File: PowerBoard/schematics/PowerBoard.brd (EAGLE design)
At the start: 200 x 100 mm, 28 parts, among them IC1 LM317MB, IC2 LM317MB, T1 TIP31C, T2 TIP31C, T3 TIP32C, X1 22-27-2031-03, X2 22-27-2031-03

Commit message: power distribution with regulators and capacitance multipliers
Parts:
- removed C1, C2: .1uF, resistor:C025-025X050
- removed C3: 1uF, resistor:E3,5-8
- removed C4, C5, C6: 100uF, resistor:E3,5-8
- removed IC3: (no value), v-reg:337TL
- removed R4: 2K, resistor:0207/7
- removed R5: 730R, resistor:0207/7
- removed R6: 1.35K, resistor:0207/7
- removed R7, R8, R9: 1K, resistor:0207/7
- added C100, C200: .1uF, rcl:C0603
- added C101, C201, C301: 100uF, rcl:153CLV-0810
- added C300: 1uF, rcl:153CLV-0810
- added IC4: 337IMP, linear:SOT223
- added LED1, LED2, LED3: (no value), led:CHIPLED_1206
- added R100: 2K, Rebel:0603
- added R101, R201: 220R, Rebel:0603
- added R102, R202, R302: 1K, Rebel:0603
- added R200: 730R, Rebel:0603
- added R300: 1.35K, Rebel:0603
- added R301: 150R, Rebel:0603
- IC1, IC2: value LM317MB -> LM317MSTT3; device v-reg:TO220L1 -> v-reg:SOT223
- R1, R2: value 220R -> 1K; device resistor:0207/7 -> Rebel:0603
- R3: value 150R -> 1K; device resistor:0207/7 -> Rebel:0603
- moved R3 203.6 mm to (147.3, 2.54), turned to 180 degrees
- moved R2 192.8 mm to (147.3, 6.35), turned to 180 degrees
- moved R1 182.0 mm to (147.3, 10.2), turned to 180 degrees
- moved T1 43.4 mm to (17.8, 20.3)
- moved IC2 42.6 mm to (59.7, 31.8)
- moved T3 38.2 mm to (95.2, 20.3)
- moved IC1 6.35 mm to (12.7, 31.8)
- moved T2 4.02 mm to (55.9, 20.3)
- moved X1 1.27 mm to (3.81, 6.35)
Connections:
- new net N$1: LED1.A, R1.2
- new net N$2: LED2.A, R2.2
- new net N$9: LED3.C, R3.2
- net +12V: now also LED1.C
- net +15V: now also C100.1, C200.1; no longer C1.1, C2.1
- net +5V: now also LED2.C
- net -12V: now also LED3.A
- net -15V: now also C300.-, IC4.4; no longer C3.-, IC3.2
- net 0V: now also C100.2, C101.-, C200.2, C201.-, C300.+, C301.-, R1.1, R100.1, R2.1, R200.1, R3.1, R300.2; no longer C1.2, C2.2, C3.+, C4.-, C5.-, C6.-, R4.1, R5.1, R6.2
- net N$10: now also C101.+, R102.1; no longer C4.+, R7.1
- net N$11: now also C201.+, R202.1; no longer C5.+, R8.1
- net N$12: now also C301.+, R302.2; no longer C6.+, R9.2
- net N$3: now also R100.2, R101.1; no longer R1.1, R4.2
- net N$4: now also R200.2, R201.1; no longer R2.1, R5.2
- net N$5: now also IC4.1, R300.1, R301.2; no longer IC3.1, R3.2, R6.1
- net N$6: now also IC1.4, R101.2, R102.2; no longer IC1.2, R1.2, R7.2
- net N$7: now also IC2.4, R201.2, R202.2; no longer IC2.2, R2.2, R8.2
- net N$8: now also IC4.3, R301.1, R302.1; no longer IC3.3, R3.1, R9.1
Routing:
- added copper zone on layer 1, net N$13
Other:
- board size 200 x 100 mm -> 200 x 53 mm

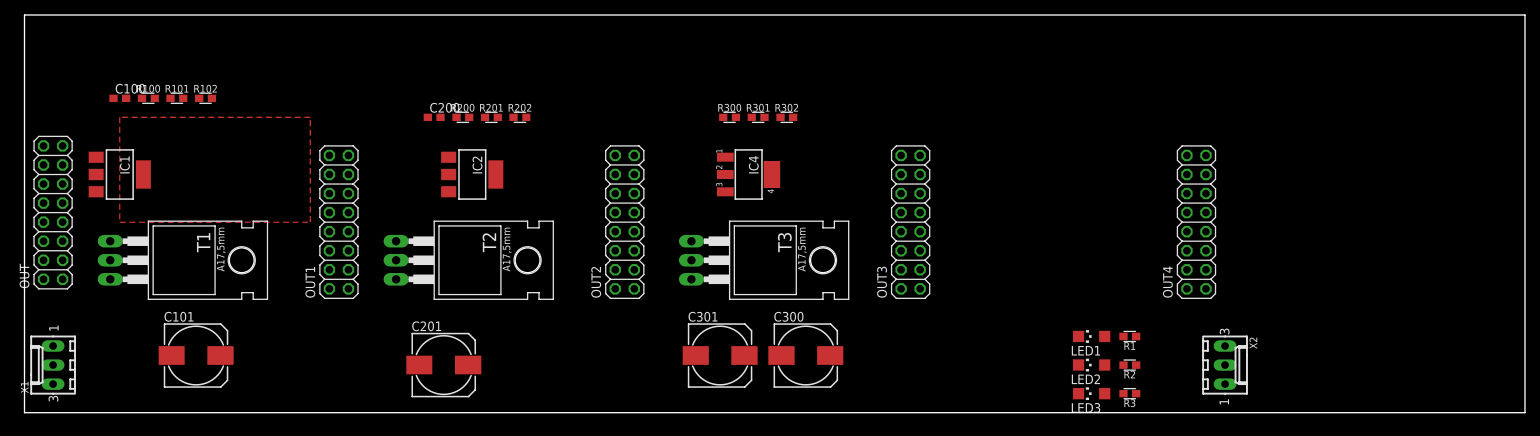
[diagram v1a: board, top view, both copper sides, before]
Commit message: changed to DPACK, 140mm long board
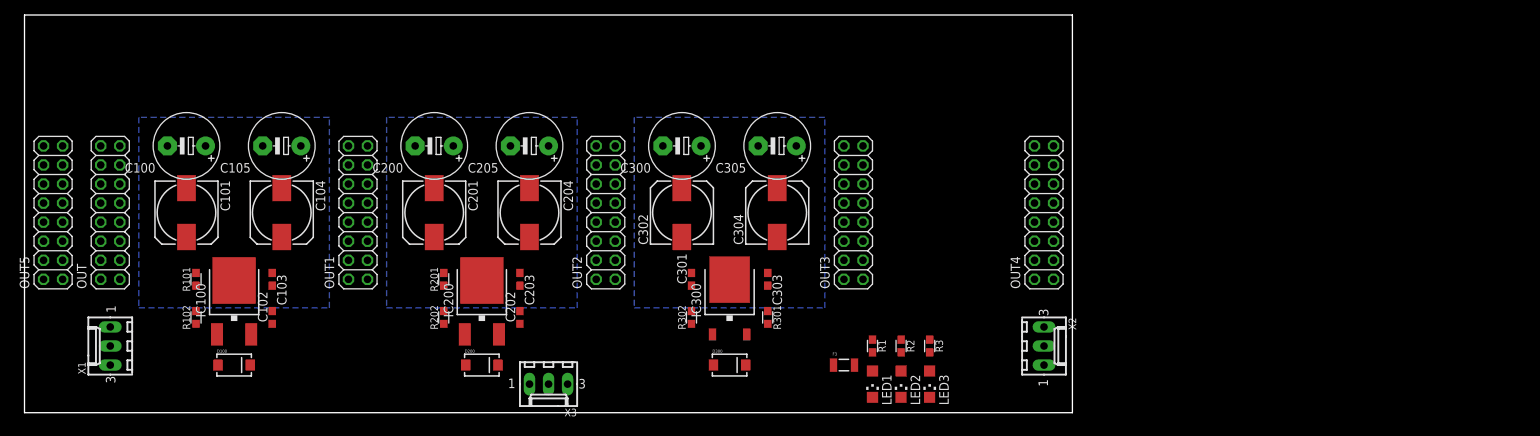
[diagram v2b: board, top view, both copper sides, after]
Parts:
- removed IC1, IC2: LM317MSTT3, v-reg:SOT223
- removed IC4: 337IMP, linear:SOT223
- removed R100: 2K, Rebel:0603
- removed R200: 730R, Rebel:0603
- removed R300: 1.35K, Rebel:0603
- removed T1, T2: TIP31C, transistor:TO220
- removed T3: TIP32C, transistor:TO220
- added C102, C202, C303: 100n, rcl:C0603
- added C103, C203: 1u, rcl:C0603
- added C104, C204, C304: 1u, rcl:153CLV-0810
- added C105, C205, C305: (no value), rcl:E5-8,5
- added C302: 10u, rcl:153CLV-0810
- added D100, D200, D300: (no value), SparkFun:SMA-DIODE
- added F3: PTCSMD, SparkFun:PTC-1206
- added IC100, IC200: LM317MABDT, v-reg:DPACK
- added IC300: 337, linear:TO252
- added OUT5: M08X2, SparkFun:2X8
- added X3: 22-27-2031-03, con-molex:6410-03
- C100, C200: value .1uF -> (none); device rcl:C0603 -> rcl:E5-8,5
- C101, C201: value 100uF -> 1u
- C300: value 1uF -> (none); device rcl:153CLV-0810 -> rcl:E5-8,5
- C301: value 100uF -> 100n; device rcl:153CLV-0810 -> rcl:C0603
- R102: value 1K -> 2K
- R202: value 1K -> 730R
- R302: value 1K -> 1.35K
- moved R1 34.3 mm to (113.0, 8.89), turned to 270 degrees
- moved C300 32.5 mm to (87.6, 35.6), turned to 180 degrees
- moved R2 30.6 mm to (116.8, 8.89), turned to 270 degrees
- moved LED1 29.9 mm to (113.0, 3.81), turned to 180 degrees
- moved R302 29.5 mm to (88.9, 12.7), turned to 90 degrees
- moved R102 29.2 mm to (22.9, 12.7), turned to 90 degrees
- moved R202 28.5 mm to (55.9, 12.7), turned to 90 degrees
- moved R3 27.4 mm to (120.7, 8.89), turned to 270 degrees
- moved R301 26.7 mm to (99.1, 12.7), turned to 270 degrees
- moved LED2 25.5 mm to (116.8, 3.81), turned to 180 degrees
- moved X2 24.3 mm to (135.9, 8.89)
- moved R101 24.3 mm to (22.9, 17.8), turned to 90 degrees
- moved R201 22.5 mm to (55.9, 17.8), turned to 90 degrees
- moved LED3 21.6 mm to (120.7, 3.81), turned to 180 degrees
- moved C201 20.4 mm to (54.6, 26.7), turned to 270 degrees
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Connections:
- removed net N$10: C101.+, R102.1, T1.1
- removed net N$11: C201.+, R202.1, T2.1
- removed net N$12: C301.+, R302.2, T3.1
- net +12V: now also C103.1, C104.+, C105.+, IC100.4, OUT5.10, OUT5.9, R101.2; no longer T1.3
- net +15V: now also D100.A, D200.A, X1.1, X3.3; no longer C100.1, C200.1, X1.3
- net +5V: now also C203.1, C204.+, C205.+, IC200.4, OUT5.11, OUT5.12, R201.2; no longer T2.3
- net -12V: now also C303.2, C304.-, C305.-, F3.2, IC300.3, OUT5.1, OUT5.2, R301.1; no longer T3.3
- net -15V: now also D300.C, X1.3, X3.1; no longer C300.-, IC4.4, X1.1
- net 0V: now also C100.-, C102.2, C103.2, C104.-, C105.-, C200.-, C202.2, C203.2, C204.-, C205.-, C301.1, C302.+, C303.1, C304.+, C305.+, R102.1, R202.1, R302.2, X3.2; no longer C100.2, C200.2, C301.-, R100.1, R200.1, R300.2
- net GND: now also OUT5.3, OUT5.4, OUT5.5, OUT5.6, OUT5.7, OUT5.8
- net N$3: now also IC100.1, R102.2; no longer IC1.1, R100.2
- net N$4: now also IC200.1, R202.2; no longer IC2.1, R200.2
- net N$5: now also IC300.1, R302.1; no longer IC4.1, R300.1
- net N$6: now also C300.-, C301.2, C302.-, D300.A, IC300.2; no longer IC1.4, R101.2, R102.2, T1.2
- net N$7: now also C200.+, C201.+, C202.1, D200.C, IC200.3; no longer IC2.4, R201.2, R202.2
- net N$8: now also C100.+, C101.+, C102.1, D100.C, IC100.3; no longer IC4.3, R301.1, R302.1, T3.2
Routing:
- added copper zone on layer 16, net N$13
- removed copper zone on layer 1, net N$13
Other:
- board size 200 x 53 mm -> 139.7 x 53 mm

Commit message: routed and labelled
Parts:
- removed F3: PTCSMD, SparkFun:PTC-1206
- added U$1, U$10, U$11, U$12, U$13, U$2, U$3, U$4, U$5, U$6, U$7, U$8, U$9: (no value), holes:3,2
- added X4: 22-27-2031-03, con-molex:6410-03
- moved X3 49.5 mm to (119.4, 3.81)
- moved LED2 27.1 mm to (121.9, 30.5), turned to 90 degrees
- moved LED1 25.7 mm to (121.9, 27.9), turned to 90 degrees
- moved R2 23.9 mm to (127.0, 30.5), turned to 180 degrees
- moved R1 23.6 mm to (127.0, 27.9), turned to 180 degrees
- moved LED3 14.0 mm to (121.9, 17.8), turned to 270 degrees
- moved D300 13.7 mm to (101.6, 17.8)
- moved C200 12.7 mm to (67.3, 35.6)
- moved C201 12.7 mm to (67.3, 26.7)
- moved C204 12.7 mm to (54.6, 26.7)
- moved C205 12.7 mm to (54.6, 35.6)
- moved C100 12.7 mm to (34.3, 35.6)
- moved C101 12.7 mm to (34.3, 26.7)
- moved C104 12.7 mm to (21.6, 26.7)
- moved C105 12.7 mm to (21.6, 35.6)
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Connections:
- removed net 0V: C100.-, C101.-, C102.2, C103.2, C104.-, C105.-, C200.-, C201.-, C202.2, C203.2, C204.-, C205.-, C300.+, C301.1, C302.+, C303.1, C304.+, C305.+, R1.1, R102.1, R2.1, R202.1, R3.1, R302.2, X1.2, X2.2, X3.2
- net +15V: now also X3.1, X4.3; no longer X3.3
- net -12V: now also IC300.2; no longer F3.2, IC300.3
- net -15V: now also X3.3, X4.1; no longer X3.1
- net GND: now also C100.-, C101.-, C102.2, C103.2, C104.-, C105.-, C200.-, C201.-, C202.2, C203.2, C204.-, C205.-, C300.+, C301.1, C302.+, C303.1, C304.+, C305.+, R1.1, R102.1, R2.1, R202.1, R3.1, R302.2, X1.2, X2.2, X3.2, X4.2
- net N$6: now also IC300.3; no longer IC300.2
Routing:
- net GND: track 0.00 -> 378.3 mm, vias 0 -> 13
- net +5V: track 0.00 -> 225.5 mm, vias 0 -> 34
- net -12V: track 0.00 -> 218.8 mm, vias 0 -> 7
- net +12V: track 0.00 -> 187.7 mm, vias 0 -> 35
- net -15V: track 0.00 -> 184.8 mm, vias 0 -> 2
- net +15V: track 0.00 -> 177.5 mm, vias 0 -> 3
- net N$8: track 0.00 -> 32.5 mm
- net N$7: track 0.00 -> 32.3 mm
- net N$3: track 0.00 -> 9.36 mm
- net N$4: track 0.00 -> 9.23 mm
- net N$5: track 0.00 -> 7.15 mm
- net N$9: track 0.00 -> 2.48 mm
- net N$2: track 0.00 -> 2.48 mm
- net N$1: track 0.00 -> 2.48 mm
- added copper zone on layer 1, net +12V
- added copper zone on layer 16, net +12V
- added copper zone on layer 1, net +5V
- added copper zone on layer 16, net +5V
- added copper zone on layer 16, net GND
- added copper zone on layer 1, net N$6
- added copper zone on layer 16, net N$6
- removed copper zone on layer 16, net N$13
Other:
- board size 139.7 x 53 mm -> 139.7 x 44.1 mm
- board text added: "+12v"
- board text added: "+15v"
- board text added: "+5v"
- board text added: "-12v"
- board text added: "-15v"
- board text added: "PowerBoard"
- board text added: "Rebel"
- board text added: "Rev01"
- board text added: "Technology"
- board text added: "gnd"

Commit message: updated values
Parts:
- C101, C104, C201, C204, C304: value 1u -> 100u
- C302: value 10u -> 100u
- C303: value 100n -> 1u
- R102: value 2K -> 2k
- R301: value 150R -> 220R
- R302: value 1.35K -> 2k
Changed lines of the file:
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@@
 <attribute name="NAME" x="54.61" y="17.018" size="1.016" layer="25" font="vector" rot="R180" align="bottom-center"/>
 </element>
-<element name="R301" library="Rebel" package="0603" value="150R" x="87.63" y="10.16" smashed="yes">
+<element name="R301" library="Rebel" package="0603" value="220R" x="87.63" y="10.16" smashed="yes">
 <attribute name="NAME" x="87.63" y="8.382" size="1.016" layer="25" font="vector" align="bottom-center"/>
 </element>
-<element name="R102" library="Rebel" package="0603" value="2K" x="21.59" y="13.97" smashed="yes">
+<element name="R102" library="Rebel" package="0603" value="2k" x="21.59" y="13.97" smashed="yes">
 <attribute name="NAME" x="21.59" y="11.557" size="1.016" layer="25" font="vector" align="bottom-center"/>
 </element>
@@
 <attribute name="NAME" x="54.61" y="13.208" size="1.016" layer="25" font="vector" rot="R180" align="bottom-center"/>
 </element>
-<element name="R302" library="Rebel" package="0603" value="1.35K" x="87.63" y="13.97" smashed="yes" rot="R180">
+<element name="R302" library="Rebel" package="0603" value="2k" x="87.63" y="13.97" smashed="yes" rot="R180">
 <attribute name="NAME" x="87.63" y="13.208" size="1.016" layer="25" font="vector" rot="R180" align="bottom-center"/>
 </element>
-<element name="C302" library="rcl" package="153CLV-0810" value="10u" x="87.63" y="26.67" smashed="yes" rot="R90">
+<element name="C302" library="rcl" package="153CLV-0810" value="100u" x="87.63" y="26.67" smashed="yes" rot="R90">
 <attribute name="NAME" x="93.26" y="24.285" size="1.27" layer="25" rot="R90"/>
 <attribute name="VALUE" x="93.415" y="22.345" size="1.27" layer="27" rot="R90"/>
 </element>
-<element name="C104" library="rcl" package="153CLV-0810" value="1u" x="21.59" y="26.67" smashed="yes" rot="R270">
+<element name="C104" library="rcl" package="153CLV-0810" value="100u" x="21.59" y="26.67" smashed="yes" rot="R270">
 <attribute name="NAME" x="27.22" y="24.285" size="1.27" layer="25" rot="R90"/>
 <attribute name="VALUE" x="15.805" y="30.995" size="1.27" layer="27" rot="R270"/>
 </element>
-<element name="C204" library="rcl" package="153CLV-0810" value="1u" x="54.61" y="26.67" smashed="yes" rot="R270">
+<element name="C204" library="rcl" package="153CLV-0810" value="100u" x="54.61" y="26.67" smashed="yes" rot="R270">
 <attribute name="NAME" x="60.24" y="24.285" size="1.27" layer="25" rot="R90"/>
 <attribute name="VALUE" x="48.825" y="30.995" size="1.27" layer="27" rot="R270"/>
 </element>
-<element name="C304" library="rcl" package="153CLV-0810" value="1u" x="100.33" y="26.67" smashed="yes" rot="R90">
+<element name="C304" library="rcl" package="153CLV-0810" value="100u" x="100.33" y="26.67" smashed="yes" rot="R90">
 <attribute name="NAME" x="105.96" y="24.285" size="1.27" layer="25" rot="R90"/>
 <attribute name="VALUE" x="106.115" y="22.345" size="1.27" layer="27" rot="R90"/>
@@
 <attribute name="VALUE" x="69.596" y="8.509" size="0.4064" layer="27" rot="R180"/>
 </element>
-<element name="C101" library="rcl" package="153CLV-0810" value="1u" x="34.29" y="26.67" smashed="yes" rot="R270">
+<element name="C101" library="rcl" package="153CLV-0810" value="100u" x="34.29" y="26.67" smashed="yes" rot="R270">
 <attribute name="NAME" x="39.92" y="24.285" size="1.27" layer="25" rot="R90"/>
 <attribute name="VALUE" x="28.505" y="30.995" size="1.27" layer="27" rot="R270"/>
 </element>
-<element name="C201" library="rcl" package="153CLV-0810" value="1u" x="67.31" y="26.67" smashed="yes" rot="R270">
+<element name="C201" library="rcl" package="153CLV-0810" value="100u" x="67.31" y="26.67" smashed="yes" rot="R270">
 <attribute name="NAME" x="72.94" y="24.285" size="1.27" layer="25" rot="R90"/>
 <attribute name="VALUE" x="61.525" y="30.995" size="1.27" layer="27" rot="R270"/>
@@
 <attribute name="VALUE" x="86.995" y="15.875" size="1.27" layer="27"/>
 </element>
-<element name="C303" library="rcl" package="C0603" value="100n" x="101.6" y="13.97" smashed="yes" rot="R180">
+<element name="C303" library="rcl" package="C0603" value="1u" x="101.6" y="13.97" smashed="yes" rot="R180">
 <attribute name="NAME" x="103.505" y="13.335" size="1.016" layer="25" rot="R180"/>
 <attribute name="VALUE" x="102.235" y="15.875" size="1.27" layer="27" rot="R180"/>
